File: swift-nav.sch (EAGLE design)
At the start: 111 parts, among them J1 SMA, J3 SMA, J4 PIN_HDR_EDG_1.27MM_5-2, J5 CON_UART3, J6 ZX62-B-5PA, J8 CON_UART1, U1 6SLX9FTG256, U10 MAX2769, U12 PT7M8206B33TA5EX, U13 M25PX80, U2 LTC3407A, U3 STM32-M-64-LQFP, U4 7Q-16.368MBG-T, U8 B4050, X3 FPGA_DEBUG_HDR

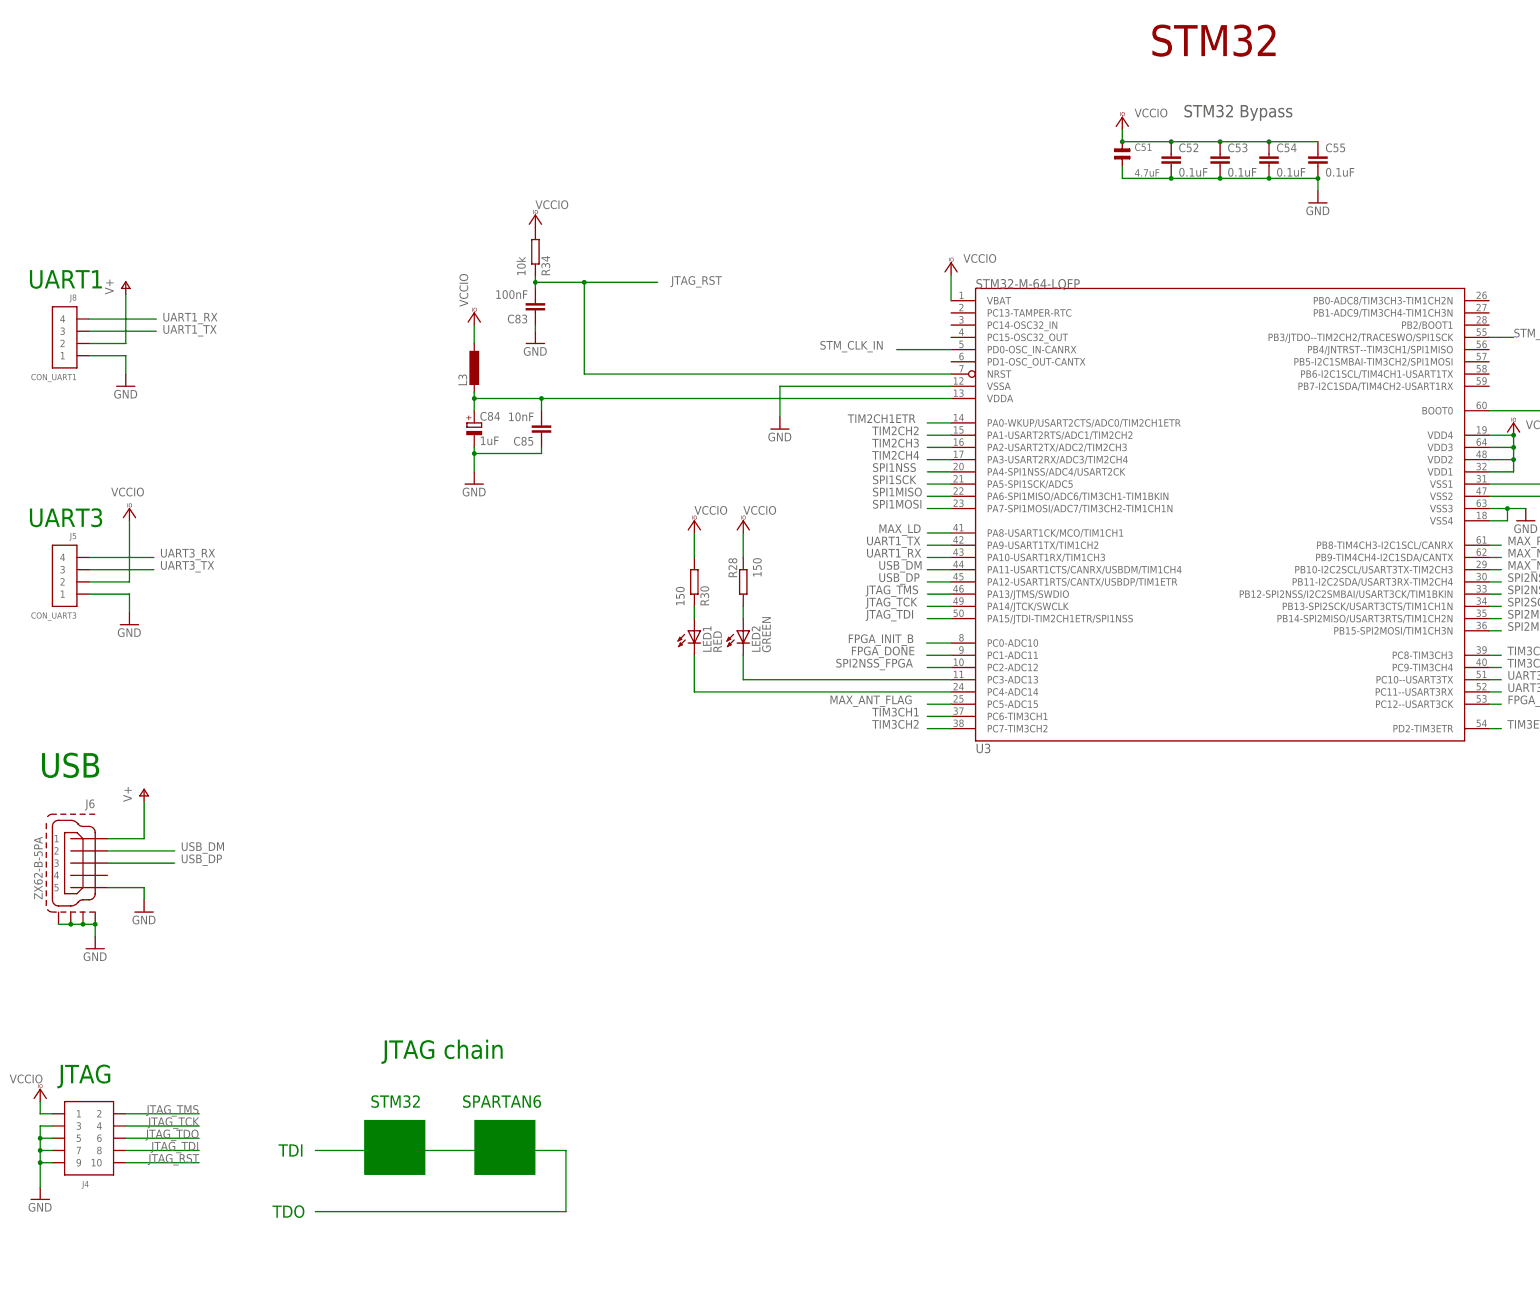
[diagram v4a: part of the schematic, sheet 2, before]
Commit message: Removed ferrite leading to VDDA pin on STM Changed UART headers to 5 pin with both 3v3 and V+ pins Changed STM32-LQFP64 symbol to F4 (VCAP_1 and VCAP_2 replace VSS1 and VSS2)
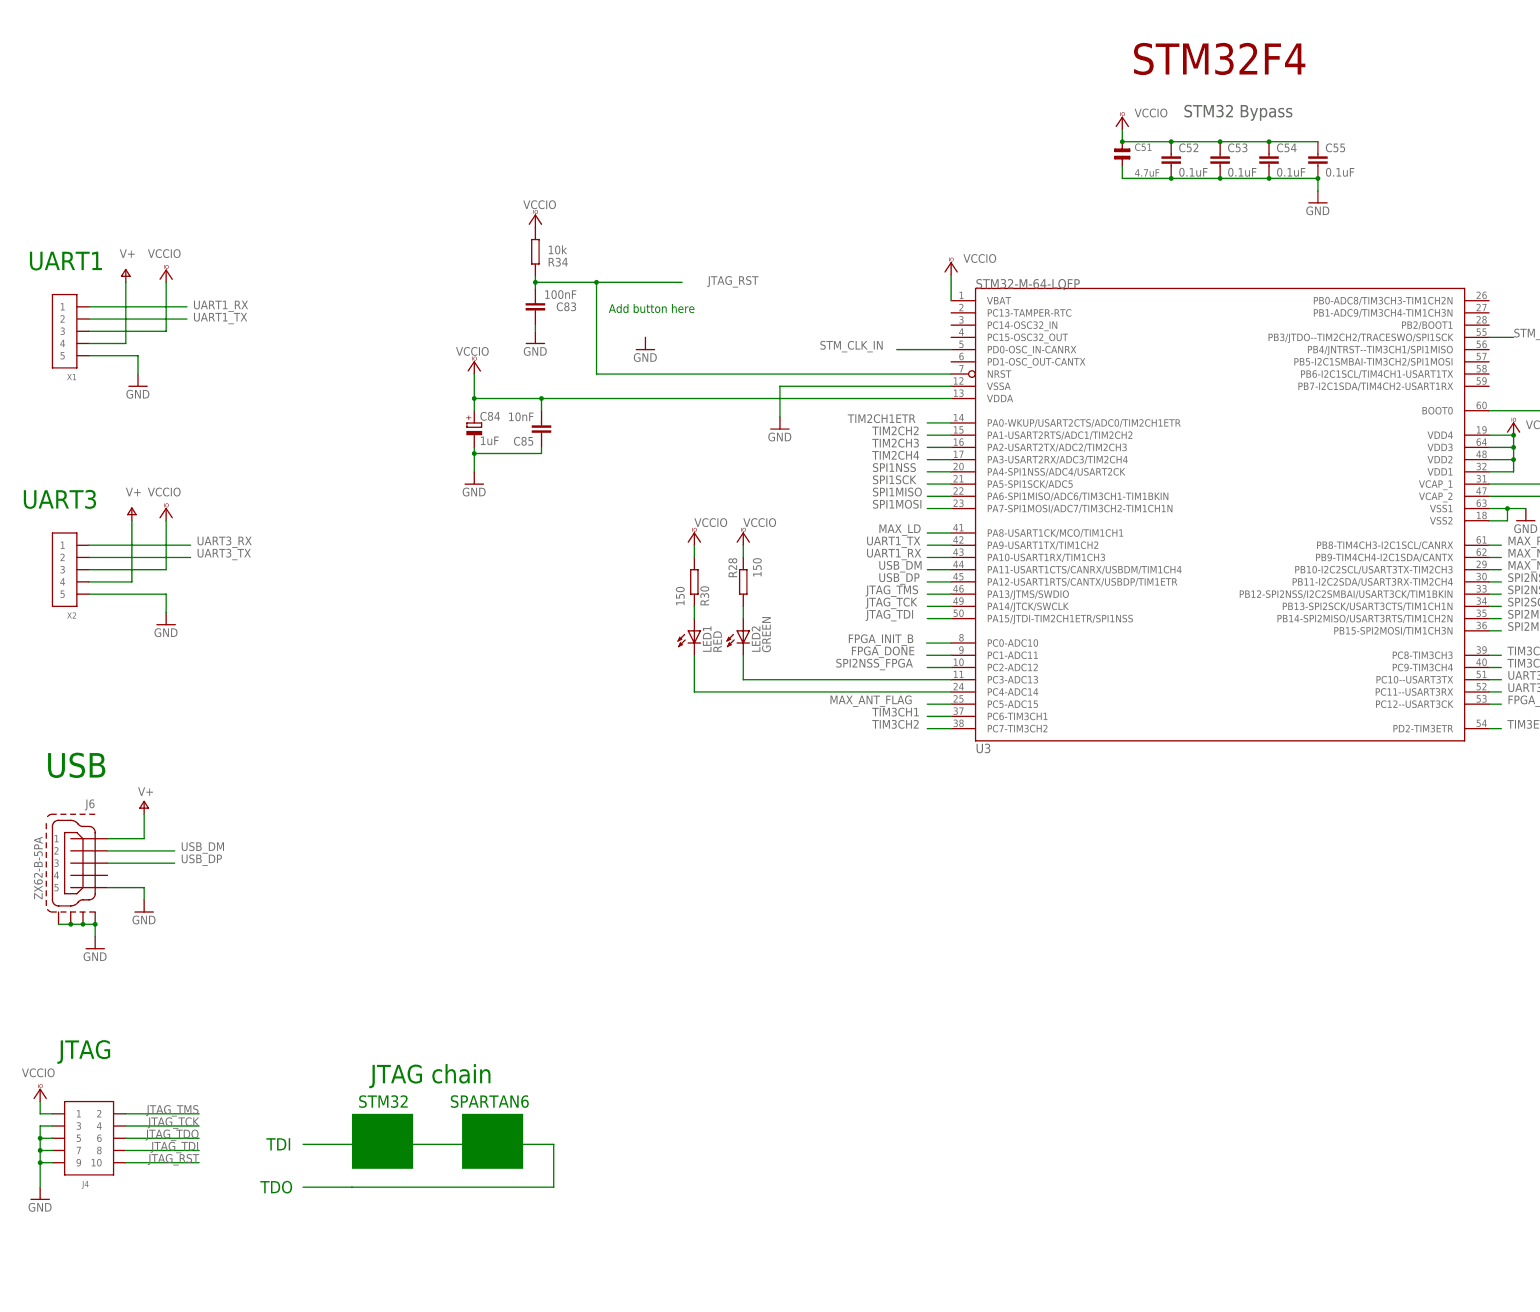
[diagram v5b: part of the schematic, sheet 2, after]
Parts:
- removed J5: CON_UART3, pel_molex:CONN_4-1-53398
- removed J8: CON_UART1, pel_molex:CONN_4-1-53398
- removed L3: INDUCTOR-0603, res_cap:INDUCTOR-0603
- added X1, X2: (no value), pel_molex:CONN_5-1-53261
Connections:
- removed net VDDA: C84.+, C85.2, L3.2, U3.VDDA
- net GND: now also U3.VSS1, U3.VSS2, X1.5, X2.5; no longer J5.1, J8.1, U3.VSS3, U3.VSS4
- net UART1_RX: now also X1.1; no longer J8.4
- net UART1_TX: now also X1.2; no longer J8.3
- net UART3_RX: now also X2.1; no longer J5.4
- net UART3_TX: now also X2.2; no longer J5.3
- net V+: now also X1.4, X2.4; no longer J8.2
- net VCCIO: now also C84.+, C85.2, U3.VDDA, X1.3, X2.3; no longer J5.2, L3.1
- net VSS1: now also U3.VCAP_1; no longer U3.VSS1
- net VSS2: now also U3.VCAP_2; no longer U3.VSS2
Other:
- note added: "Add button here"
- note added: "STM32F4"

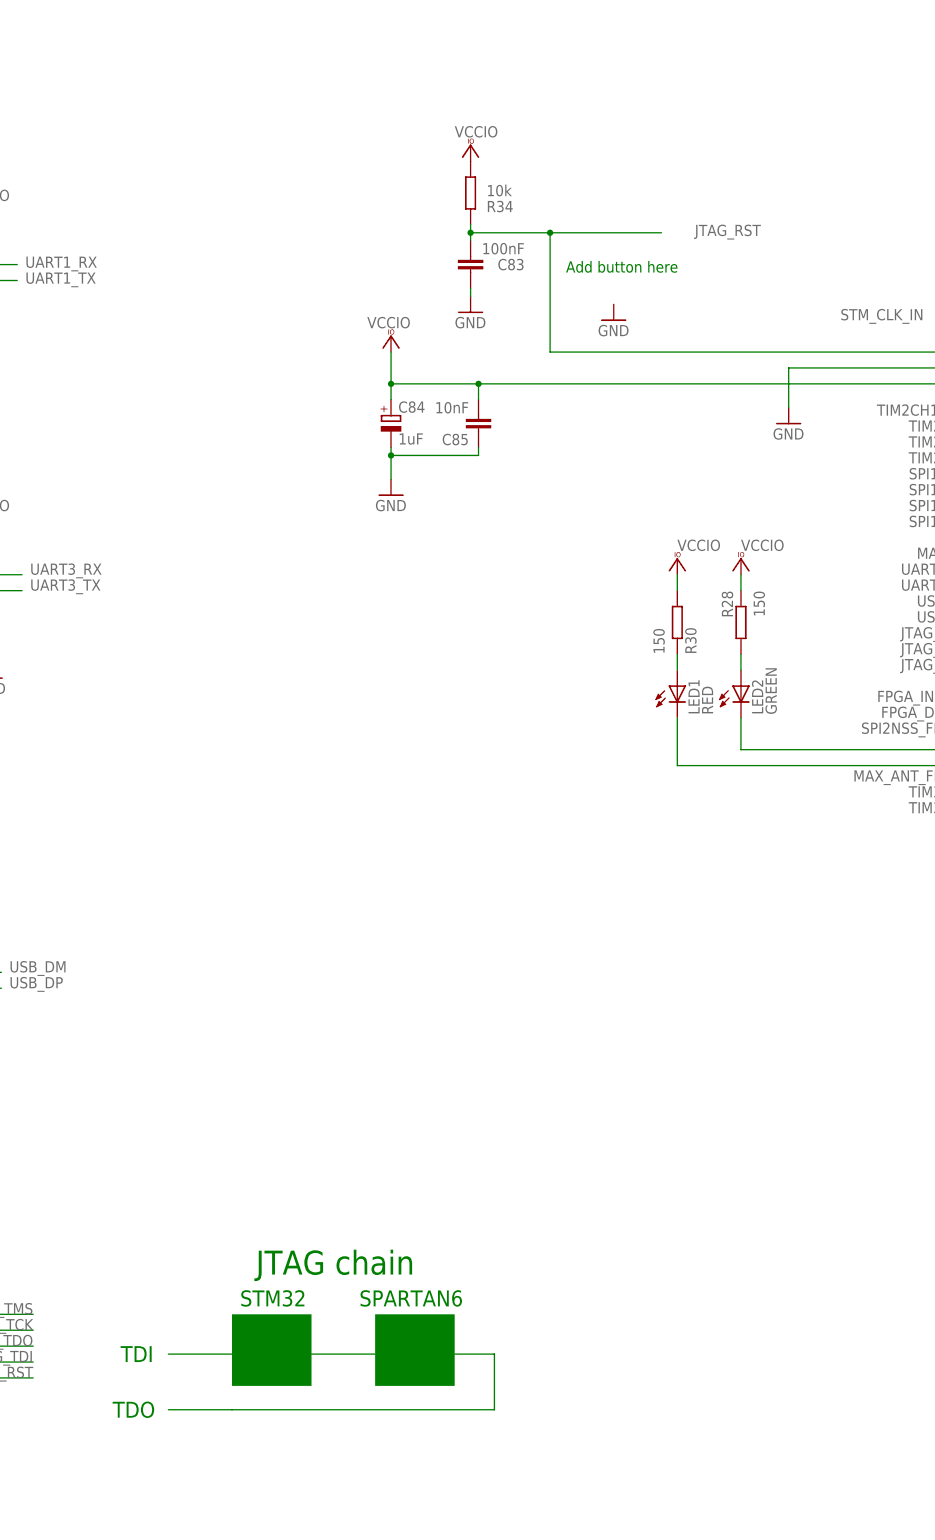
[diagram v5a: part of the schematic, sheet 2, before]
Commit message: Added button to JTAG_RST line Added libraries used in design of 2.1
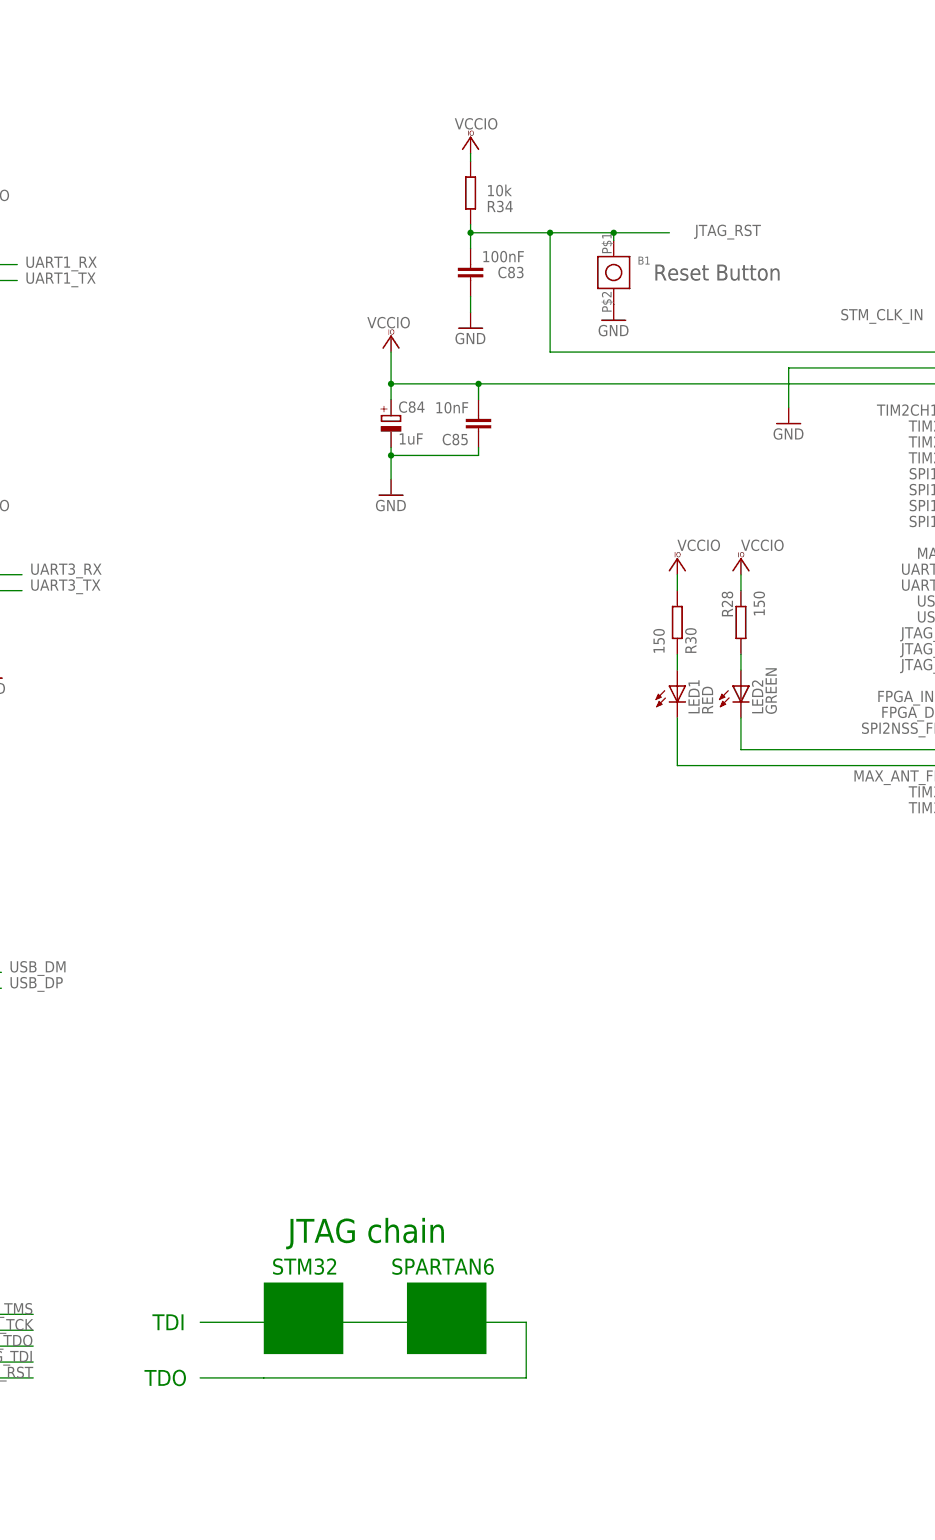
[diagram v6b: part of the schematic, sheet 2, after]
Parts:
- added B1: B3U-1000P, jobygnss:B3U-1000P
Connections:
- net GND: now also B1.2
- net JTAG_RST: now also B1.1
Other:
- note added: "Reset Button"
- note removed: "Add button here"
- moved on the sheet: C83
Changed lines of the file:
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@@
 <setting verticaltext="up"/>
 </settings>
-<grid distance="0.05" unitdist="inch" unit="inch" style="lines" multiple="1" display="yes" altdistance="0.01" altunitdist="inch" altunit="inch"/>
+<grid distance="0.1" unitdist="inch" unit="inch" style="lines" multiple="1" display="no" altdistance="0.01" altunitdist="inch" altunit="inch"/>
 <layers>
 <layer number="1" name="Top" color="4" fill="1" visible="no" active="no"/>
@@
 <part name="P+6" library="supply1" deviceset="V+" device=""/>
 <part name="VCC8" library="supply1" deviceset="VCCIO" device=""/>
+<part name="B1" library="jobygnss" deviceset="B3U-1000P" device=""/>
 </parts>
 <sheets>
@@
 <text x="24.13" y="322.58" size="3.81" layer="91" rot="MR180">UART1</text>
 <text x="22.86" y="273.05" size="3.81" layer="91" rot="MR180">UART3</text>
-<text x="95.25" y="153.67" size="3.81" layer="91" rot="MR180">JTAG chain</text>
-<rectangle x1="91.44" y1="132.08" x2="104.14" y2="143.51" layer="91"/>
-<rectangle x1="114.3" y1="132.08" x2="127" y2="143.51" layer="91"/>
-<text x="73.66" y="135.89" size="2.54" layer="91">TDI</text>
-<text x="72.39" y="127" size="2.54" layer="91">TDO</text>
-<text x="92.71" y="144.78" size="2.54" layer="91">STM32</text>
-<text x="111.76" y="144.78" size="2.54" layer="91">SPARTAN6</text>
+<text x="100.33" y="158.75" size="3.81" layer="91" rot="MR180">JTAG chain</text>
+<rectangle x1="96.52" y1="137.16" x2="109.22" y2="148.59" layer="91"/>
+<rectangle x1="119.38" y1="137.16" x2="132.08" y2="148.59" layer="91"/>
+<text x="78.74" y="140.97" size="2.54" layer="91">TDI</text>
+<text x="77.47" y="132.08" size="2.54" layer="91">TDO</text>
+<text x="97.79" y="149.86" size="2.54" layer="91">STM32</text>
+<text x="116.84" y="149.86" size="2.54" layer="91">SPARTAN6</text>
 <text x="454.66" y="27.94" size="5.08" layer="94">STM32 / CONNECTORS</text>
 <text x="543.56" y="5.715" size="3.81" layer="94">2.2</text>
 <text x="433.705" y="355.6" size="3.81" layer="97">Outer RF shield</text>
-<text x="144.78" y="309.88" size="1.778" layer="91">Add button here</text>
+<text x="158.75" y="308.61" size="2.54" layer="97">Reset Button</text>
 </plain>
 <instances>
@@
 <attribute name="VALUE" x="218.44" y="320.294" size="1.778" layer="96"/>
 </instance>
-<instance part="C83" gate="G$1" x="129.54" y="309.88" smashed="yes" rot="R180">
-<attribute name="NAME" x="138.176" y="312.039" size="1.778" layer="95" rot="R180"/>
-<attribute name="VALUE" x="138.176" y="314.579" size="1.778" layer="96" rot="R180"/>
+<instance part="C83" gate="G$1" x="129.54" y="308.61" smashed="yes" rot="R180">
+<attribute name="NAME" x="138.176" y="310.769" size="1.778" layer="95" rot="R180"/>
+<attribute name="VALUE" x="138.176" y="313.309" size="1.778" layer="96" rot="R180"/>
 </instance>
 <instance part="C84" gate="G$1" x="116.84" y="287.02"/>
@@
 <attribute name="NAME" x="132.08" y="319.532" size="1.778" layer="95"/>
 </instance>
-<instance part="VCC30" gate="G$1" x="129.54" y="330.2" smashed="yes">
-<attribute name="VALUE" x="127" y="331.47" size="1.778" layer="96"/>
+<instance part="VCC30" gate="G$1" x="129.54" y="331.47" smashed="yes">
+<attribute name="VALUE" x="127" y="332.74" size="1.778" layer="96"/>
 </instance>
 <instance part="GND59" gate="1" x="180.34" y="285.75"/>
-<instance part="GND57" gate="1" x="129.54" y="303.53"/>
+<instance part="GND57" gate="1" x="129.54" y="300.99"/>
 <instance part="VCC32" gate="G$1" x="116.84" y="299.72" smashed="yes">
 <attribute name="VALUE" x="113.03" y="300.99" size="1.778" layer="96"/>
@@
 <attribute name="VALUE" x="49.022" y="321.31" size="1.778" layer="96"/>
 </instance>
+<instance part="B1" gate="G$1" x="149.86" y="312.42" smashed="yes" rot="R270">
+<attribute name="NAME" x="156.21" y="311.15" size="1.27" layer="95"/>
+</instance>
 </instances>
 <busses>
@@
 </segment>
 <segment>
-<wire x1="129.54" y1="307.34" x2="129.54" y2="306.07" width="0.1524" layer="91"/>
+<wire x1="129.54" y1="306.07" x2="129.54" y2="303.53" width="0.1524" layer="91"/>
 <pinref part="C83" gate="G$1" pin="1"/>
 <pinref part="GND57" gate="1" pin="GND"/>
@@
 <wire x1="347.98" y1="289.56" x2="347.98" y2="288.925" width="0.1524" layer="91"/>
 </segment>
+<segment>
+<pinref part="B1" gate="G$1" pin="2"/>
+<pinref part="GND3" gate="1" pin="GND"/>
+</segment>
 </net>
 <net name="VCCIO" class="0">
@@
 <pinref part="R34" gate="G$1" pin="2"/>
 <pinref part="VCC30" gate="G$1" pin="VCCIO"/>
+<wire x1="129.54" y1="328.93" x2="129.54" y2="327.66" width="0.1524" layer="91"/>
 </segment>
 <segment>
@@
 <wire x1="129.54" y1="316.23" x2="142.24" y2="316.23" width="0.1524" layer="91"/>
 <wire x1="129.54" y1="317.5" x2="129.54" y2="316.23" width="0.1524" layer="91"/>
-<wire x1="129.54" y1="316.23" x2="129.54" y2="314.96" width="0.1524" layer="91"/>
+<wire x1="129.54" y1="316.23" x2="129.54" y2="313.69" width="0.1524" layer="91"/>
 <wire x1="142.24" y1="316.23" x2="142.24" y2="297.18" width="0.1524" layer="91"/>
 <wire x1="142.24" y1="297.18" x2="215.9" y2="297.18" width="0.1524" layer="91"/>
@@
 <pinref part="R34" gate="G$1" pin="1"/>
 <pinref part="U3" gate="G$1" pin="NRST"/>
-<wire x1="142.24" y1="316.23" x2="160.02" y2="316.23" width="0.1524" layer="91"/>
+<wire x1="142.24" y1="316.23" x2="152.4" y2="316.23" width="0.1524" layer="91"/>
 <junction x="142.24" y="316.23"/>
+<pinref part="B1" gate="G$1" pin="1"/>
+<wire x1="152.4" y1="316.23" x2="161.29" y2="316.23" width="0.1524" layer="91"/>
+<wire x1="152.4" y1="314.96" x2="152.4" y2="316.23" width="0.1524" layer="91"/>
+<junction x="152.4" y="316.23"/>
 </segment>
 </net>
@@
 <net name="N$1" class="0">
 <segment>
-<wire x1="81.28" y1="137.16" x2="91.44" y2="137.16" width="0.1524" layer="91"/>
+<wire x1="86.36" y1="142.24" x2="96.52" y2="142.24" width="0.1524" layer="91"/>
 </segment>
 </net>
 <net name="N$2" class="0">
 <segment>
-<wire x1="81.28" y1="128.27" x2="91.44" y2="128.27" width="0.1524" layer="91"/>
+<wire x1="86.36" y1="133.35" x2="96.52" y2="133.35" width="0.1524" layer="91"/>
 </segment>
 </net>
 <net name="N$12" class="0">
 <segment>
-<wire x1="104.14" y1="137.16" x2="114.3" y2="137.16" width="0.1524" layer="91"/>
+<wire x1="109.22" y1="142.24" x2="119.38" y2="142.24" width="0.1524" layer="91"/>
 </segment>
 </net>
 <net name="N$13" class="0">
 <segment>
-<wire x1="127" y1="137.16" x2="133.35" y2="137.16" width="0.1524" layer="91"/>
-<wire x1="133.35" y1="137.16" x2="133.35" y2="128.27" width="0.1524" layer="91"/>
-<wire x1="133.35" y1="128.27" x2="91.44" y2="128.27" width="0.1524" layer="91"/>
+<wire x1="132.08" y1="142.24" x2="138.43" y2="142.24" width="0.1524" layer="91"/>
+<wire x1="138.43" y1="142.24" x2="138.43" y2="133.35" width="0.1524" layer="91"/>
+<wire x1="138.43" y1="133.35" x2="96.52" y2="133.35" width="0.1524" layer="91"/>
 </segment>
 </net>
